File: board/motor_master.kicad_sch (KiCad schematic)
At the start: 38 parts, among them IC1 LM1117MPX-3.3_NOPB, IC2 SN65HVD232DR, J1 PWR, J2 USB4105-GF-A, J3 FTDI, J4 CAN, J5 TERM, J6 PWM1, J7 PWM2, U1 ESP32-S3-WROOM-1-N8

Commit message: Board revisions from design review
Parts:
- removed R7: 120, Resistor_SMD:R_0603_1608Metric, symbol Device:R_Small_US
- added C13: 0.1uF, Capacitor_SMD:C_0603_1608Metric, symbol Device:C
- added C14: 4.7n, Capacitor_SMD:C_0603_1608Metric, symbol Device:C
- added C15, C9: 100p, Capacitor_SMD:C_0603_1608Metric, symbol Device:C
- added D5: 150060RS75000, SamacSys_Parts:LEDC1608X80N, symbol SamacSys_Parts:150060RS75000
- added D6: SZNUP2105LT1G, SamacSys_Parts:SOT96P237X111-3N, symbol SamacSys_Parts:SZNUP2105LT1G
- added J1: EXT, SamacSys_Parts:TSW-102-XX-YY-S, symbol SamacSys_Parts:TSW-102-07-T-S
- added R10: 47, Resistor_SMD:R_0603_1608Metric, symbol Device:R_Small_US
- added R8, R9: 60, Resistor_SMD:R_1206_3216Metric, symbol Device:R_Small_US
- D2: renamed from D3; value D5V0S1U2LP-7B -> PTVS18VU1UPAZ; footprint D5V0S1U2LP7B -> SamacSys_Parts:PMEG6020EPA115; symbol SamacSys_Parts:D5V0S1U2LP-7B -> SamacSys_Parts:PTVS18VU1UPAZ; Height 0.53 -> 0.65; Manufacturer_Name Diodes Incorporated -> Nexperia; Manufacturer_Part_Number D5V0S1U2LP-7B -> PTVS18VU1UPAZ; Mouser Part Number 621-D5V0S1U2LP-7B -> 771-PTVS18VU1UPAZ; Mouser Price/Stock https://www.mouser.co.uk/ProductDetail/Diodes-Incorporated/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 -> https://www.mouser.co.uk/ProductDetail/Nexperia/PTVS18VU1UP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; Supplier_Number 621-D5V0S1U2LP-7B -> 771-PTVS18VU1UPAZ
- D4: value D5V0S1U2LP-7B -> PTVS18VU1UPAZ; footprint D5V0S1U2LP7B -> SamacSys_Parts:PMEG6020EPA115; symbol SamacSys_Parts:D5V0S1U2LP-7B -> SamacSys_Parts:PTVS18VU1UPAZ; Height 0.53 -> 0.65; Manufacturer_Name Diodes Incorporated -> Nexperia; Manufacturer_Part_Number D5V0S1U2LP-7B -> PTVS18VU1UPAZ; Mouser Part Number 621-D5V0S1U2LP-7B -> 771-PTVS18VU1UPAZ; Mouser Price/Stock https://www.mouser.co.uk/ProductDetail/Diodes-Incorporated/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 -> https://www.mouser.co.uk/ProductDetail/Nexperia/PTVS18VU1UP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; Supplier_Number 621-D5V0S1U2LP-7B -> 771-PTVS18VU1UPAZ
- IC2: footprint SOIC127P600X175-8N -> SamacSys_Parts:SOIC127P600X175-8N
- J2: renamed from J3; footprint HDRV4W64P0X254_1X4_1016X254X889P -> SamacSys_Parts:HDRV4W64P0X254_1X4_1016X254X889P
- J4, J6, J7: footprint SamacSys_Parts:TSW-103-XX-YY-S -> SamacSys_Parts:1719710103
- J5: renamed from J1; value PWR -> 5-12V; footprint SamacSys_Parts:SHDR2W70P0X500_1X2_1000X750X1160P -> SamacSys_Parts:1190297; symbol SamacSys_Parts:691137710002 -> SamacSys_Parts:1190297; Height 11.6 -> 23.58; Manufacturer_Name Wurth Elektronik -> Phoenix Contact; Manufacturer_Part_Number 691137710002 -> 1190297; Mouser Part Number 710-691137710002 -> 651-1190297; Mouser Price/Stock https://www.mouser.co.uk/ProductDetail/Wurth-Elektronik/691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 -> https://www.mouser.co.uk/ProductDetail/Phoenix-Contact/1190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; Supplier_Number 710-691137710002 -> 651-1190297
- J8: renamed from J5; footprint SamacSys_Parts:RHDR3W79P0X254_1X3_813X241X851P -> SamacSys_Parts:1719710103
- R1: renamed from R3; value 5.1k -> 47; Supplier_Number 71-CRCW0603-5.1K-E3 -> 71-CRCW0603-47-E3
- S1: renamed from S4; footprint PTS636SKG25JSMTRLFS -> SamacSys_Parts:PTS636SKG25JSMTRLFS
- S2: renamed from S3; footprint PTS636SKG25JSMTRLFS -> SamacSys_Parts:PTS636SKG25JSMTRLFS
- S3: renamed from S1; footprint PTS636SKG25JSMTRLFS -> SamacSys_Parts:PTS636SKG25JSMTRLFS
- renumbered C2 to C1, C11 to C10, C8 to C11, C9 to C12, C1 to C2, C7 to C3, C6 to C4, C4 to C5, C5 to C6, C10 to C7, C3 to C8, D2 to D3, J2 to J3, R6 to R11, R8 to R2, R2 to R3, R1 to R4, R9 to R6, R4 to R7, S2 to S4
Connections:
- net GND: now also J4.2 (NC), J5.3 (-), J5.4 (-), J8.2 (NC), C13.1, C14.1, C15.2, C9.2, D5.2 (A), D6.3 (GND), J1.2; no longer J5.2 (-)
- net VCC_3V3: now also C13.2
- net VCC_IN: now also D2.3 (K_1), D2.4 (K_2), D4.3 (K_1), D4.4 (K_2), J5.2 (+); no longer D2.1 (K), D4.1 (K)
- net at D2.2 (A_2), D3.1 (IO1), J3.A4_B9 (VBUS)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: now also D2.1 (A_1)
- net at IC2.6 (CANL), J4.3 (CANL): now also C15.1, D6.2 (CANL), R8.2
- net at IC2.7 (CANH), J4.1 (CANH): now also C9.1, D6.1 (CANH), R9.2
- net GPIO9: now reaches U1.17 (IO9)
- net GPIO9: now also IC2.1 (D)
- net GPIO10: now reaches U1.18 (IO10)
- net GPIO10: now also IC2.4 (R)
- net GPIO11: now reaches U1.19 (IO11)
- net GPIO11: now also R10.2
- net GPIO21: now reaches U1.23 (IO21)
- net GPIO21: now also J6.1 (SIG)
- net GPIO47: now reaches U1.24 (IO47)
- net GPIO47: now also J7.1 (SIG)
- net GPIO48: now reaches U1.25 (IO48)
- net GPIO48: now also C11.2, R7.1, S4.2, S4.4
- net GPIO2: now reaches U1.38 (IO2)
- net GPIO2: now also C7.2, R2.1, S1.2 (NO)
- net GPIO1: now reaches U1.39 (IO1)
- net GPIO1: now also J1.1
- net at D4.2 (A_2), J2.2: now also D4.1 (A_1)
- net GPIO12: no longer names the net of U1.20 (IO12)
- net GPIO12: no longer IC2.1 (D)
- net GPIO13: no longer names the net of U1.21 (IO13)
- net GPIO13: no longer IC2.4 (R)
- removed net GPIO15: C11.2, R7.1, S4.2, S4.4, U1.8 (IO15)
- removed net GPIO4: C7.2, R2.1, S1.2 (NO), U1.4 (IO4)
- net GPIO5: no longer names the net of U1.5 (IO5)
- net GPIO5: no longer J6.1 (SIG)
- net GPIO6: no longer names the net of U1.6 (IO6)
- net GPIO6: no longer J7.1 (SIG)
- new net: D5.1 (K), R10.1
- new net: C14.2, R8.1, R9.1
- no-connect marks 36 -> 32
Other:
- moved on the sheet: D2, IC2, J4, J5, J8, R11

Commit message: Changed power diodes
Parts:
- removed D2, D4: PTVS18VU1UPAZ, SamacSys_Parts:PMEG6020EPA115, symbol SamacSys_Parts:PTVS18VU1UPAZ
- added D2, D4: SK14, DIONM5027X250N, symbol SamacSys_Parts:SK14
- J4, J6, J7: Supplier_Number 200-TSW10307TS -> 538-171971-0103
- J8: Supplier_Number 200-SSW10301FS -> 538-171971-0103
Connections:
- net VCC_IN: now also D2.1 (K), D4.1 (K)
- net at D3.1 (IO1), J3.A4_B9 (VBUS), J3.B4_A9 (VBUS__1): now also D2.2 (A)
- net at J2.2: now also D4.2 (A)

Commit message: Updated BOM with manufactuer numbers
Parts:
- C1, C4, C6, C8: Mfr_Number (none) -> C0603C106M9PAC
- C10, C11, C12, C13, C2, C3, C5, C7: Mfr_Number (none) -> C0603C104K5RAC3121
- C14: Mfr_Number (none) -> C0603C472J5GACTU
- C15, C9: Mfr_Number (none) -> C0603C101J1GAC7411
- D1, D5: Mfr_Number (none) -> 150060RS75000
- D2, D4: Manufacturer_Part_Number SK14 -> (none); Mfr_Number (none) -> SK14
- D3: Manufacturer_Part_Number TPD4E02B04DQAR -> (none); Mfr_Number (none) -> TPD4E02B04DQAR
- D6: Manufacturer_Part_Number SZNUP2105LT1G -> (none); Mfr_Number (none) -> SZNUP2105LT1G
- IC1: Mfr_Number (none) -> LM1117MPX-3.3/NOPB
- IC2: Manufacturer_Part_Number SN65HVD232DR -> (none); Mfr_Number (none) -> SN65HVD232DR
- J1: Manufacturer_Part_Number TSW-102-07-T-S -> (none); Mfr_Number (none) -> TSW-102-07-T-S
- J2: Mfr_Number (none) -> M20-9990446
- J3: Mfr_Number (none) -> USB4105-GF-A-120; Part_Number (none) -> USB4105-GF-A-120
- J4: Manufacturer_Part_Number TSW-103-07-T-S -> (none); Mfr_Number (none) -> 705430002; Supplier_Number 538-171971-0103 -> 538-70543-0002
- J5: Mfr_Number (none) -> 1190297
- J6, J7: Mfr_Number (none) -> 705430002; Supplier_Number 538-171971-0103 -> 538-70543-0002
- J8: Manufacturer_Part_Number SSW-103-01-F-S -> (none); Mfr_Number (none) -> 705430002; Supplier_Number 538-171971-0103 -> 538-70543-0002
- R1, R10: Mfr_Number (none) -> CRCW060347R0FKEA
- R11: Mfr_Number (none) -> CRCW0603120RFKEA
- R2, R5, R6, R7: Mfr_Number (none) -> CRCW060310K0FKEA
- R3, R4: Mfr_Number (none) -> CRCW06035K10FKEA
- R8, R9: Mfr_Number (none) -> CRCW120660R0KNAIF
- S1, S2, S3: Mfr_Number (none) -> PTS636 SKG25J SMTR LFS; Supplier_Number PTS636 SKG25J SMTR LFS -> 611-PTS636SKG25JSMTR
- S4: Mfr_Number (none) -> FSM4JH
- U1: Mfr_Number 356-ESP32-S3WROOM1N8 -> ESP32-S3-WROOM-1-N8

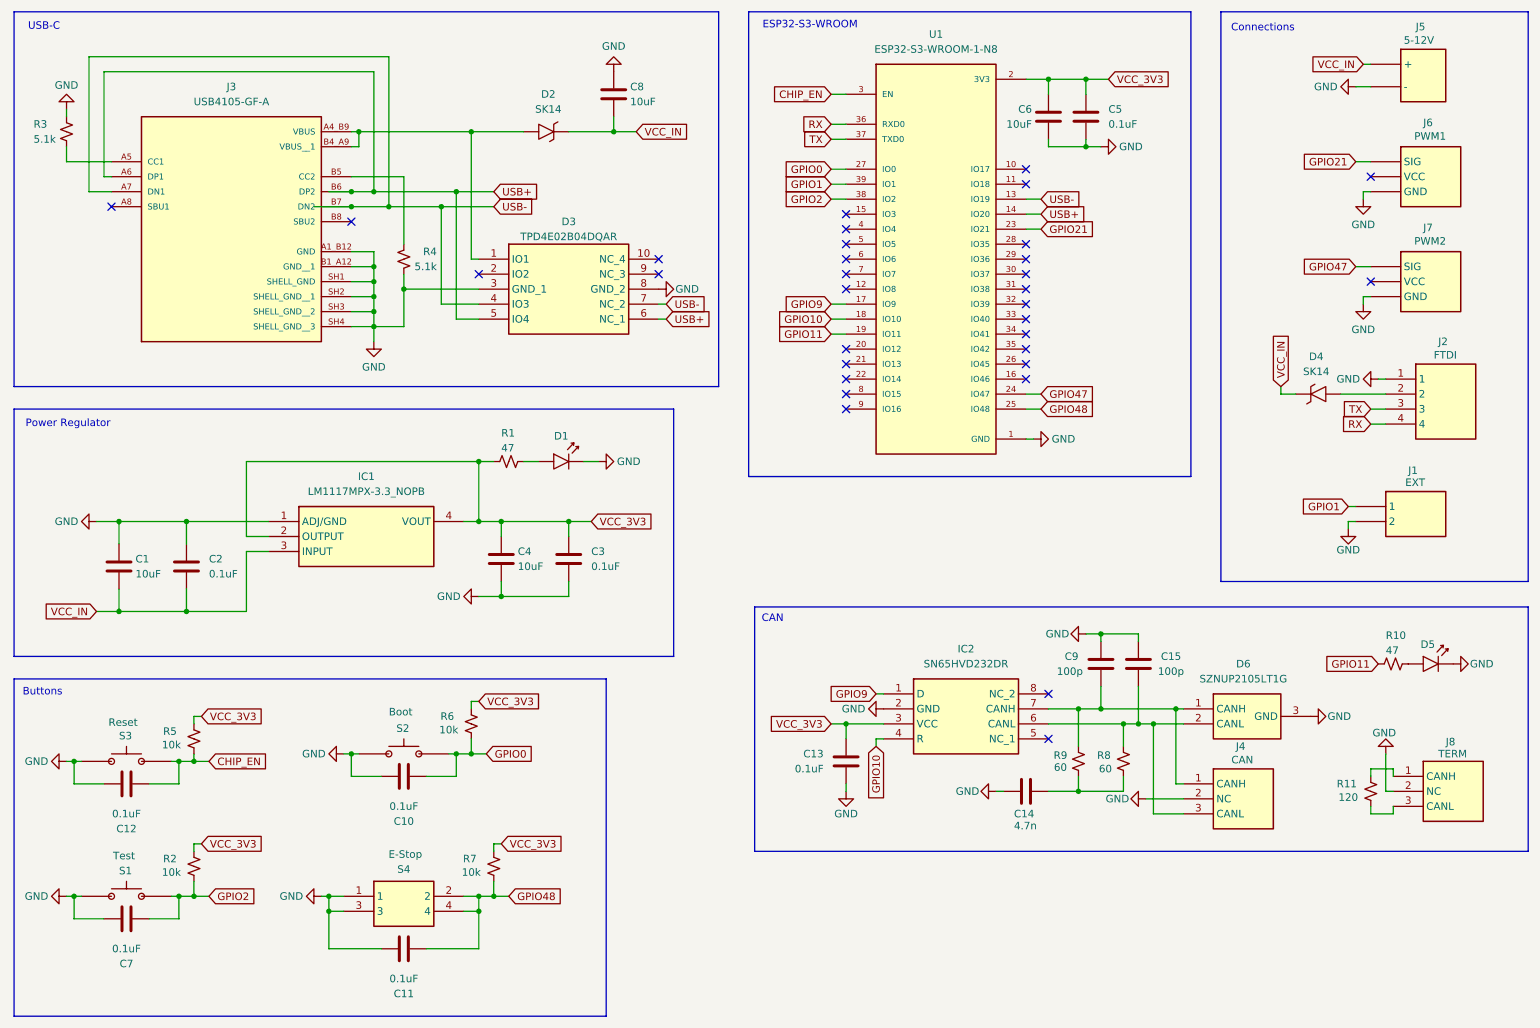
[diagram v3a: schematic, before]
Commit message: Changed LEDs and fixed estop button wiring
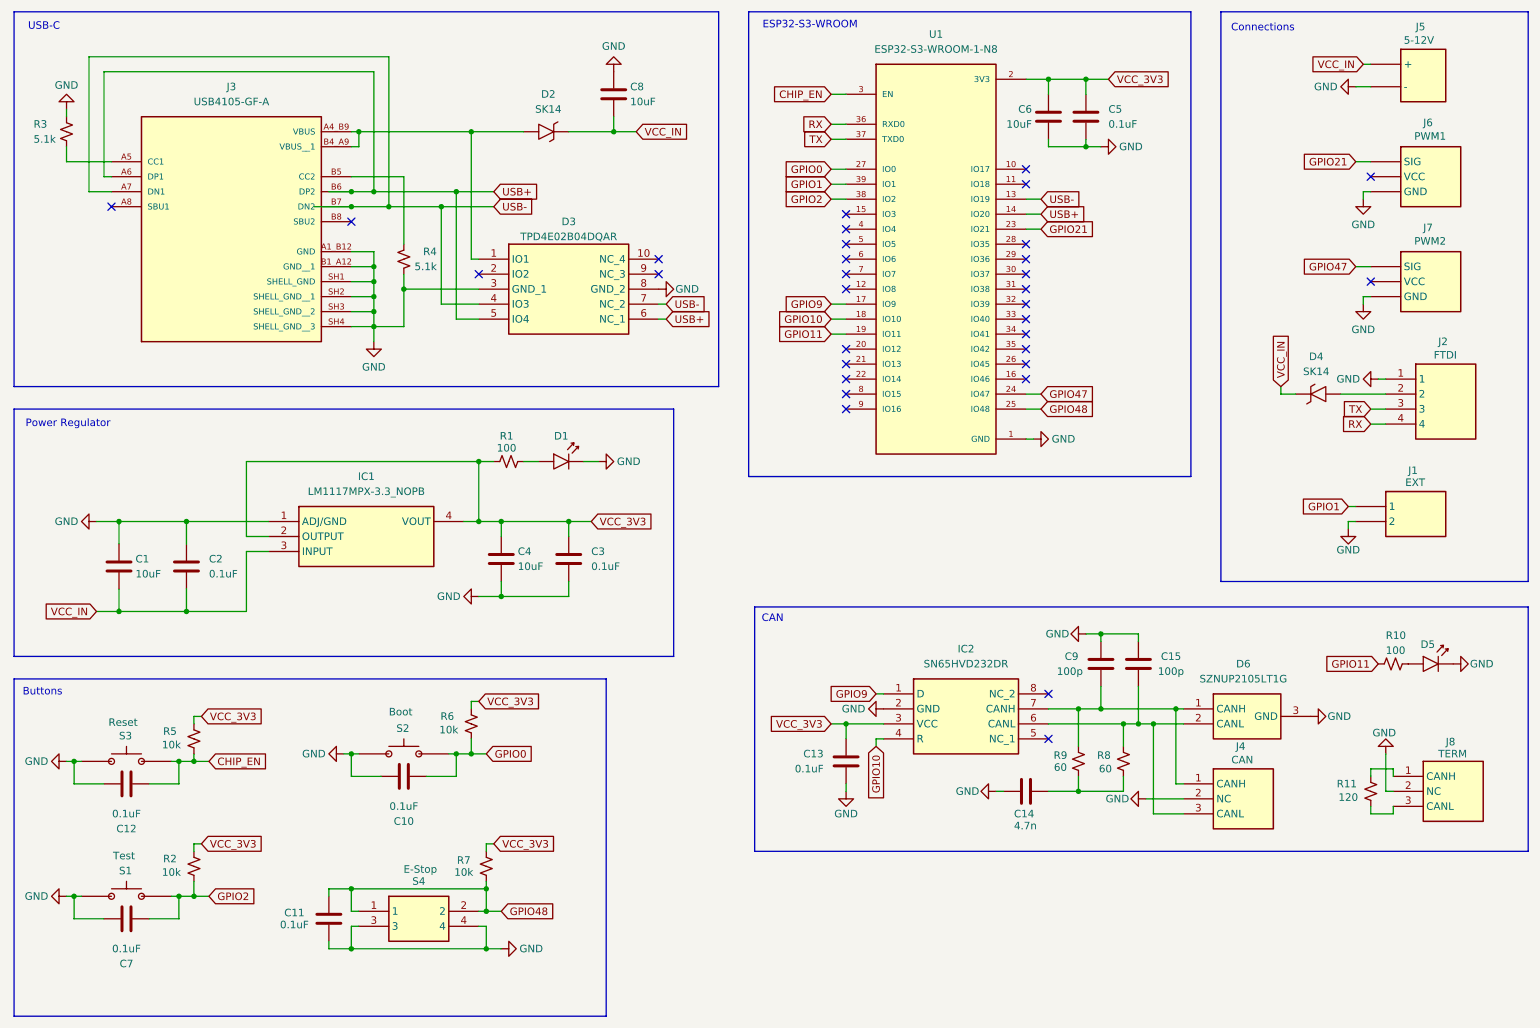
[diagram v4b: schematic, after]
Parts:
- D5: Mfr_Number 150060RS75000 -> 150060VS75000; Supplier_Number 710-150060RS75000 -> 710-150060VS75000
- R1, R10: value 47 -> 100; Mfr_Number CRCW060347R0FKEA -> CRCW0603100RFKEA; Supplier_Number 71-CRCW0603-47-E3 -> 71-CRCW0603-100-E3
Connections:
- net GND: now also C11.2, S4.4; no longer C11.1, S4.1
- net GPIO48: now also C11.1, S4.1; no longer C11.2, S4.4
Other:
- moved on the sheet: C11, R7, S4

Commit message: Added pullup resistor to extern pin, renumbered parts
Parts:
- added R8: 10k, Resistor_SMD:R_0603_1608Metric, symbol Device:R_Small_US
- renumbered C8 to C1, C6 to C10, C5 to C11, C9 to C12, C15 to C13, C13 to C14, C14 to C15, C4 to C2, C1 to C4, C2 to C5, C10 to C6, C12 to C7, C7 to C8, C11 to C9, D2 to D1, D3 to D2, D1 to D3, J3 to J1, J5 to J2, J6 to J3, J7 to J4, J2 to J5, J1 to J6, J8 to J7, J4 to J8, R3 to R1, R9 to R10, R8 to R11, R11 to R12, R4 to R2, R1 to R3, R6 to R4, R2 to R6, R10 to R9, S2 to S1, S3 to S2, S1 to S3
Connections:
- net GPIO1: now also R8.1
- net VCC_3V3: now also R8.2
